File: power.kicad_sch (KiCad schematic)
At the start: 18 parts, among them J13 Screw_Terminal_01x02, U6 LM66100DCK, U7 LM66100DCK, U8 LMR51610XDBVR, U9 TLV74033PDBVR

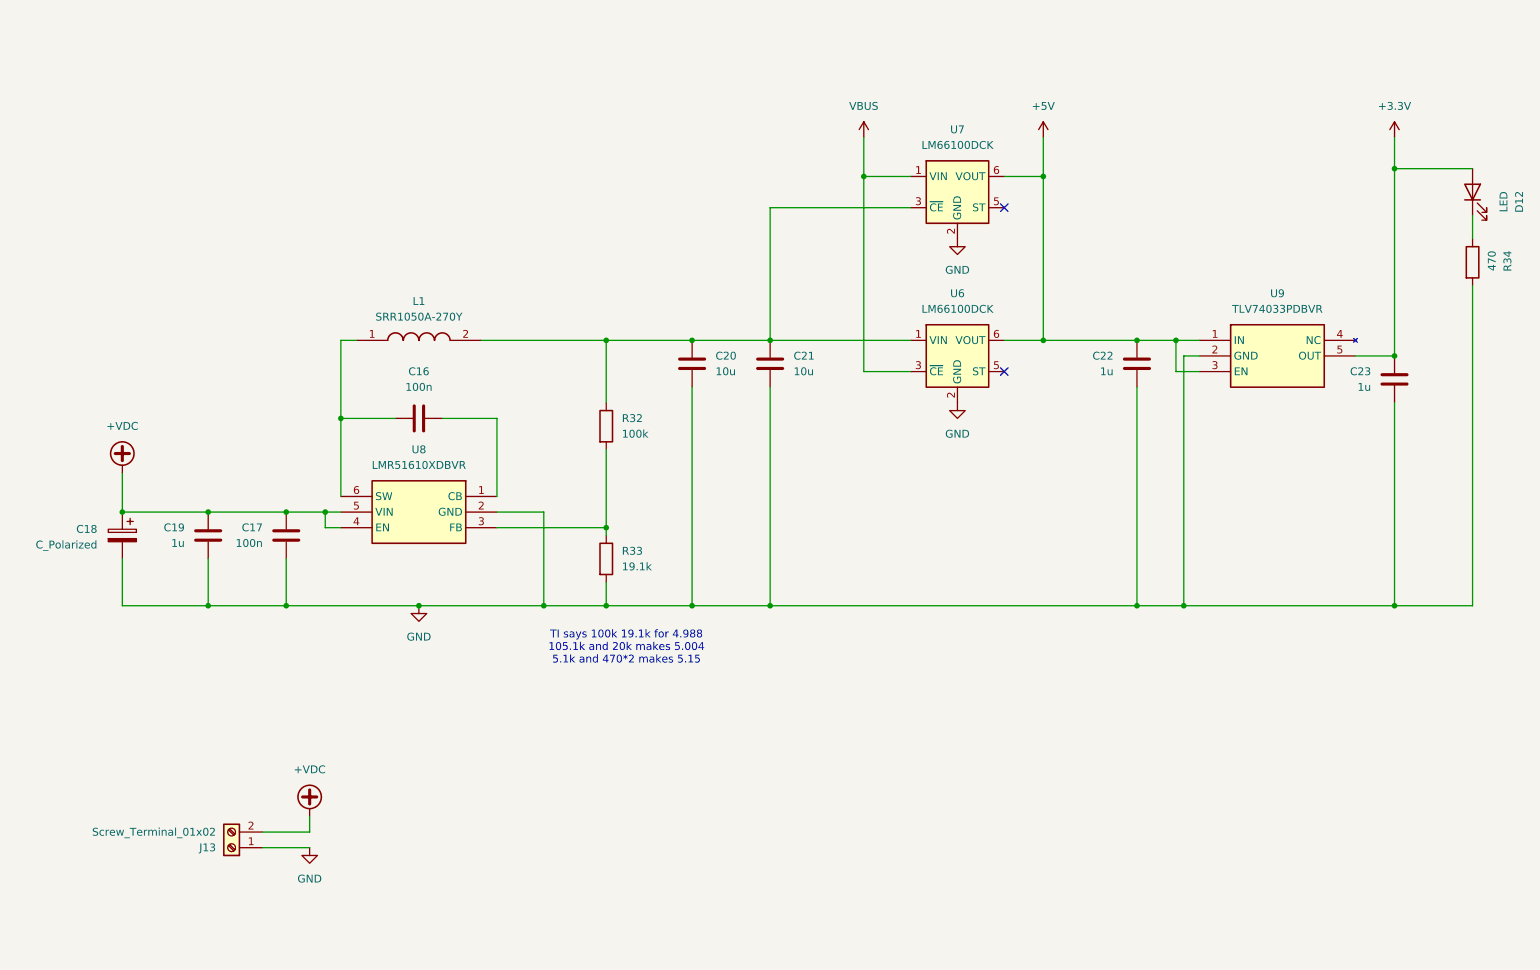
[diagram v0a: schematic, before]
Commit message: add probe headers
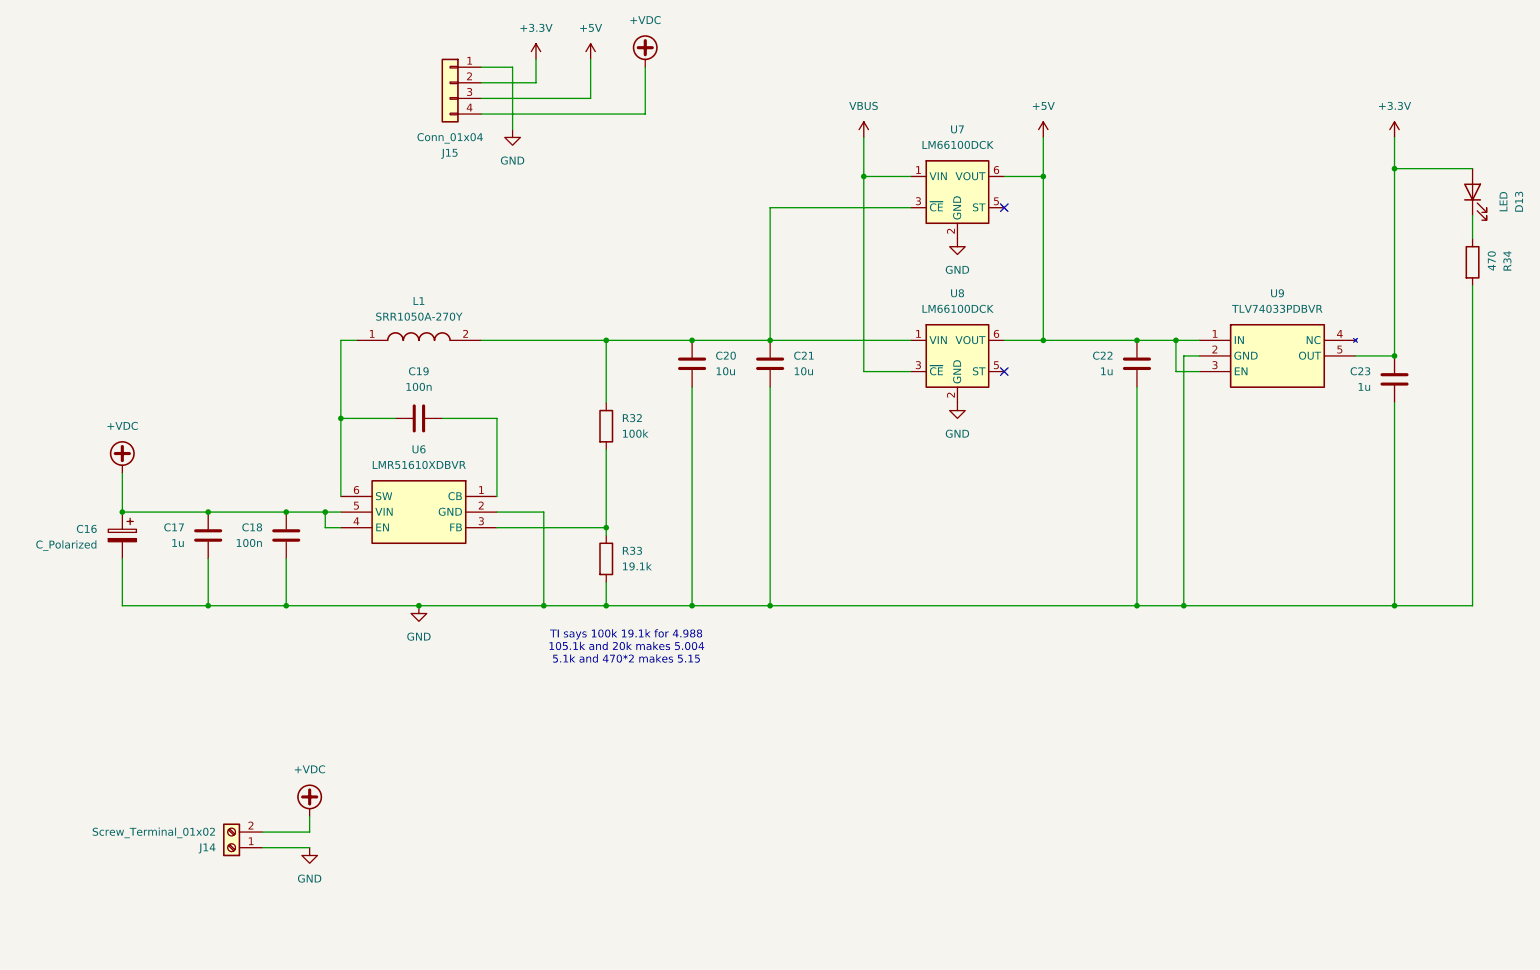
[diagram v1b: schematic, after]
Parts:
- added J15: Conn_01x04, Connector_PinHeader_2.54mm:PinHeader_1x04_P2.54mm_Vertical, symbol Connector_Generic:Conn_01x04
- renumbered C18 to C16, C19 to C17, C17 to C18, C16 to C19, D12 to D13, J13 to J14, U8 to U6, U6 to U8
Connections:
- net +3.3V: now also J15.2 (Pin_2)
- net +5V: now also J15.3 (Pin_3)
- net +VDC: now also J15.4 (Pin_4)
- net GND: now also J15.1 (Pin_1)

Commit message: partial layout
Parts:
- added C26: 100n, Capacitor_SMD:C_0603_1608Metric_Pad1.08x0.95mm_HandSolder, symbol Device:C
- added D14: MM3Zxx, Diode_SMD:D_SOD-323F, symbol Diode:MM3Zxx
- added R36: 100k, Resistor_SMD:R_0603_1608Metric_Pad0.98x0.95mm_HandSolder, symbol Device:R
- added R37: 5.1k, Resistor_SMD:R_0603_1608Metric_Pad0.98x0.95mm_HandSolder, symbol Device:R
- renumbered C16 to C18, C17 to C19, C18 to C20, C19 to C21, C20 to C22, C21 to C23, C22 to C24, C23 to C25, R32 to R33, R33 to R34, R34 to R35
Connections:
- net +VDC: now also R36.1
- net GND: now also C26.2, D14.2 (A), R37.2
- new net V_SENSE_VDC: C26.1, D14.1 (K), R36.2, R37.1

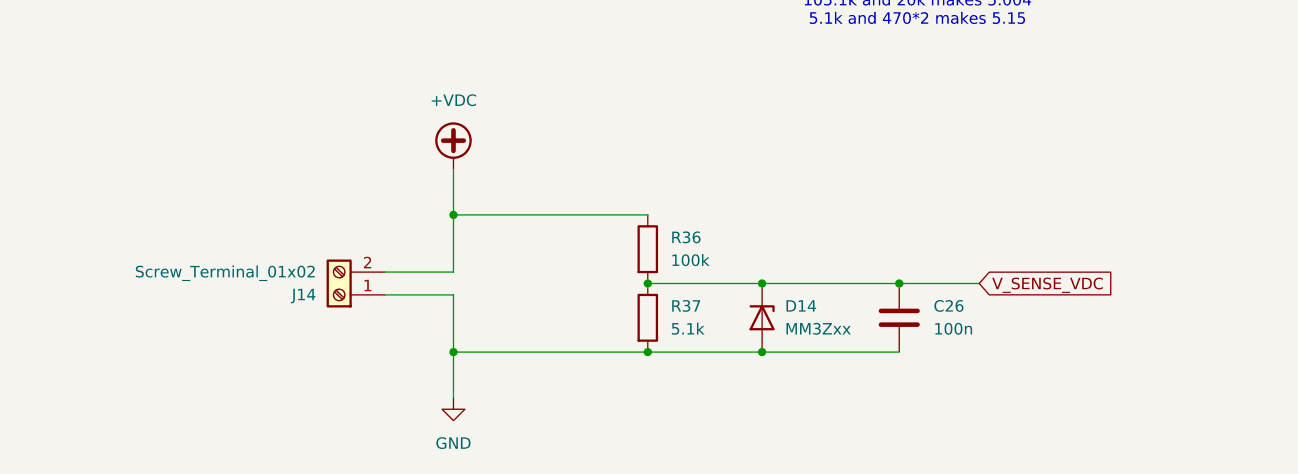
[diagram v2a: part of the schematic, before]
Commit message: schematic changes for mini
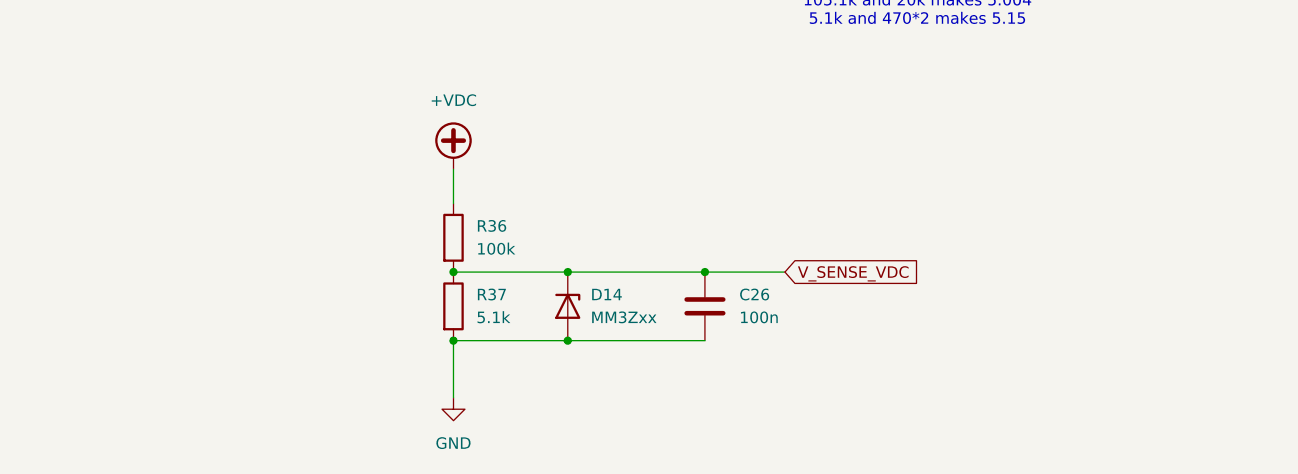
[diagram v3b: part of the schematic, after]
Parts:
- removed J14: Screw_Terminal_01x02, TerminalBlock_MetzConnect:TerminalBlock_MetzConnect_Type101_RT01602HBWC_1x02_P5.08mm_Horizontal, symbol Connector:Screw_Terminal_01x02
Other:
- moved on the sheet: C26, D14, R36, R37
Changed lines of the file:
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@@
 	)
 	(junction
-		(at 88.9 173.99)
+		(at 67.31 172.72)
 		(diameter 0)
 		(color 0 0 0 0)
@@
 	)
 	(junction
-		(at 101.6 173.99)
+		(at 80.01 172.72)
 		(diameter 0)
 		(color 0 0 0 0)
@@
 	)
 	(junction
-		(at 67.31 173.99)
-		(diameter 0)
-		(color 0 0 0 0)
-	)
-	(junction
 		(at 186.69 85.09)
 		(diameter 0)
@@
 	)
 	(junction
-		(at 116.84 166.37)
+		(at 95.25 165.1)
 		(diameter 0)
 		(color 0 0 0 0)
@@
 	)
 	(junction
-		(at 88.9 166.37)
+		(at 67.31 165.1)
 		(diameter 0)
 		(color 0 0 0 0)
@@
 	)
 	(junction
-		(at 101.6 166.37)
+		(at 80.01 165.1)
 		(diameter 0)
 		(color 0 0 0 0)
@@
 		(color 0 0 0 0)
 	)
-	(junction
-		(at 67.31 158.75)
-		(diameter 0)
-		(color 0 0 0 0)
-	)
 	(no_connect
 		(at 180.34 63.5)
@@
 	(wire
 		(pts
-			(xy 88.9 166.37) (xy 101.6 166.37)
+			(xy 67.31 165.1) (xy 80.01 165.1)
 		)
 		(stroke
@@
 	(wire
 		(pts
-			(xy 67.31 173.99) (xy 67.31 167.64)
-		)
-		(stroke
-			(width 0)
-			(type default)
-		)
-	)
-	(wire
-		(pts
 			(xy 142.24 92.71) (xy 142.24 128.27)
 		)
@@
 	(wire
 		(pts
-			(xy 59.69 165.1) (xy 67.31 165.1)
-		)
-		(stroke
-			(width 0)
-			(type default)
-		)
-	)
-	(wire
-		(pts
 			(xy 208.28 90.17) (xy 208.28 85.09)
 		)
@@
 	(wire
 		(pts
-			(xy 101.6 173.99) (xy 116.84 173.99)
+			(xy 80.01 172.72) (xy 95.25 172.72)
 		)
 		(stroke
@@
 	(wire
 		(pts
-			(xy 116.84 166.37) (xy 125.73 166.37)
+			(xy 95.25 165.1) (xy 104.14 165.1)
 		)
 		(stroke
@@
 	(wire
 		(pts
-			(xy 67.31 173.99) (xy 88.9 173.99)
-		)
-		(stroke
-			(width 0)
-			(type default)
-		)
-	)
-	(wire
-		(pts
-			(xy 67.31 158.75) (xy 67.31 153.67)
+			(xy 67.31 157.48) (xy 67.31 153.67)
 		)
 		(stroke
@@
 	(wire
 		(pts
-			(xy 67.31 165.1) (xy 67.31 158.75)
-		)
-		(stroke
-			(width 0)
-			(type default)
-		)
-	)
-	(wire
-		(pts
 			(xy 243.84 57.15) (xy 243.84 87.63)
 		)
@@
 	(wire
 		(pts
-			(xy 67.31 167.64) (xy 59.69 167.64)
-		)
-		(stroke
-			(width 0)
-			(type default)
-		)
-	)
-	(wire
-		(pts
 			(xy 180.34 85.09) (xy 186.69 85.09)
 		)
@@
 	(wire
 		(pts
-			(xy 101.6 166.37) (xy 116.84 166.37)
+			(xy 80.01 165.1) (xy 95.25 165.1)
 		)
 		(stroke
@@
 	(wire
 		(pts
-			(xy 67.31 179.07) (xy 67.31 173.99)
+			(xy 67.31 179.07) (xy 67.31 172.72)
 		)
 		(stroke
@@
 	(wire
 		(pts
-			(xy 88.9 173.99) (xy 101.6 173.99)
+			(xy 67.31 172.72) (xy 80.01 172.72)
 		)
 		(stroke
@@
 	(wire
 		(pts
-			(xy 67.31 158.75) (xy 88.9 158.75)
-		)
-		(stroke
-			(width 0)
-			(type default)
-		)
-	)
-	(wire
-		(pts
 			(xy 129.54 92.71) (xy 129.54 128.27)
 		)
@@
 	(global_label "V_SENSE_VDC"
 		(shape input)
-		(at 125.73 166.37 0)
+		(at 104.14 165.1 0)
 		(fields_autoplaced yes)
 		(effects
@@
 		)
 		(property "Intersheetrefs" "${INTERSHEET_REFS}"
-			(at 141.4151 166.37 0)
+			(at 119.8251 165.1 0)
 			(effects
 				(font
@@
 	(symbol
 		(lib_id "Diode:MM3Zxx")
-		(at 101.6 170.18 270)
+		(at 80.01 168.91 270)
 		(unit 1)
 		(exclude_from_sim no)
@@
 		(fields_autoplaced yes)
 		(property "Reference" "D14"
-			(at 104.14 168.9099 90)
+			(at 82.55 167.6399 90)
 			(effects
 				(font
@@
 		)
 		(property "Value" "MM3Zxx"
-			(at 104.14 171.4499 90)
+			(at 82.55 170.1799 90)
 			(effects
 				(font
@@
 		)
 		(property "Footprint" "Diode_SMD:D_SOD-323F"
-			(at 97.155 170.18 0)
+			(at 75.565 168.91 0)
 			(effects
 				(font
@@
 		)
 		(property "Datasheet" "https://diotec.com/tl_files/diotec/files/pdf/datasheets/mm3z2v4.pdf"
-			(at 101.6 170.18 0)
+			(at 80.01 168.91 0)
 			(effects
 				(font
@@
 		)
 		(property "Description" "300mW Zener Diode, SOD-323F"
-			(at 101.6 170.18 0)
+			(at 80.01 168.91 0)
 			(effects
 				(font
@@
 	(symbol
 		(lib_id "Device:R")
-		(at 88.9 170.18 0)
+		(at 67.31 168.91 0)
 		(unit 1)
 		(exclude_from_sim no)
@@
 		(fields_autoplaced yes)
 		(property "Reference" "R37"
-			(at 91.44 168.9099 0)
+			(at 69.85 167.6399 0)
 			(effects
 				(font
@@
 		)
 		(property "Value" "5.1k"
-			(at 91.44 171.4499 0)
+			(at 69.85 170.1799 0)
 			(effects
 				(font
@@
 		)
 		(property "Footprint" "Resistor_SMD:R_0603_1608Metric_Pad0.98x0.95mm_HandSolder"
-			(at 87.122 170.18 90)
+			(at 65.532 168.91 90)
 			(effects
 				(font
@@
 		)
 		(property "Datasheet" "~"
-			(at 88.9 170.18 0)
+			(at 67.31 168.91 0)
 			(effects
 				(font
@@
 		)
 		(property "Description" "Resistor"
-			(at 88.9 170.18 0)
+			(at 67.31 168.91 0)
 			(effects
 				(font
@@
 	(symbol
 		(lib_id "Device:C")
-		(at 116.84 170.18 0)
+		(at 95.25 168.91 0)
 		(unit 1)
 		(exclude_from_sim no)
@@
 		(fields_autoplaced yes)
 		(property "Reference" "C26"
-			(at 120.65 168.9099 0)
+			(at 99.06 167.6399 0)
 			(effects
 				(font
@@
 		)
 		(property "Value" "100n"
-			(at 120.65 171.4499 0)
+			(at 99.06 170.1799 0)
 			(effects
 				(font
@@
 		)
 		(property "Footprint" "Capacitor_SMD:C_0603_1608Metric_Pad1.08x0.95mm_HandSolder"
-			(at 117.8052 173.99 0)
+			(at 96.2152 172.72 0)
 			(effects
 				(font
@@
 		)
 		(property "Datasheet" "~"
-			(at 116.84 170.18 0)
+			(at 95.25 168.91 0)
 			(effects
 				(font
@@
 		)
 		(property "Description" "Unpolarized capacitor"
-			(at 116.84 170.18 0)
+			(at 95.25 168.91 0)
 			(effects
 				(font
@@
 	)
 	(symbol
-		(lib_id "Connector:Screw_Terminal_01x02")
-		(at 54.61 167.64 180)
-		(unit 1)
-		(exclude_from_sim no)
-		(in_bom yes)
-		(on_board yes)
-		(dnp no)
-		(property "Reference" "J14"
-			(at 52.07 167.6401 0)
-			(effects
-				(font
-					(size 1.27 1.27)
-				)
-				(justify left)
-			)
-		)
-		(property "Value" "Screw_Terminal_01x02"
-			(at 52.07 165.1001 0)
-			(effects
-				(font
-					(size 1.27 1.27)
-				)
-				(justify left)
-			)
-		)
-		(property "Footprint" "TerminalBlock_MetzConnect:TerminalBlock_MetzConnect_Type101_RT01602HBWC_1x02_P5.08mm_Horizontal"
-			(at 54.61 167.64 0)
-			(effects
-				(font
-					(size 1.27 1.27)
-				)
-				(hide yes)
-			)
-		)
-		(property "Datasheet" "~"
-			(at 54.61 167.64 0)
-			(effects
-				(font
-					(size 1.27 1.27)
-				)
-				(hide yes)
-			)
-		)
-		(property "Description" "Generic screw terminal, single row, 01x02, script generated (kicad-library-utils/schlib/autogen/connector/)"
-			(at 54.61 167.64 0)
-			(effects
-				(font
-					(size 1.27 1.27)
-				)
-				(hide yes)
-			)
-		)
-		(pin "2"
-		)
-		(pin "1"
-		)
-		(instances
-			(project "dmxdude"
-				(path "/bd7590c0-6a37-4bf0-a9f2-f26180744ceb/497bfd7a-c06a-4d4d-a320-8405be197f02"
-					(reference "J14")
-					(unit 1)
-				)
-			)
-		)
-	)
-	(symbol
 		(lib_id "Power_Management:LM66100DCK")
 		(at 172.72 60.96 0)
@@
 	(symbol
 		(lib_id "Device:R")
-		(at 88.9 162.56 0)
+		(at 67.31 161.29 0)
 		(unit 1)
 		(exclude_from_sim no)
@@
 		(fields_autoplaced yes)
 		(property "Reference" "R36"
-			(at 91.44 161.2899 0)
+			(at 69.85 160.0199 0)
 			(effects
 				(font
@@
 		)
 		(property "Value" "100k"
-			(at 91.44 163.8299 0)
+			(at 69.85 162.5599 0)
 			(effects
 				(font
@@
 		)
 		(property "Footprint" "Resistor_SMD:R_0603_1608Metric_Pad0.98x0.95mm_HandSolder"
-			(at 87.122 162.56 90)
+			(at 65.532 161.29 90)
 			(effects
 				(font
@@
 		)
 		(property "Datasheet" "~"
-			(at 88.9 162.56 0)
+			(at 67.31 161.29 0)
 			(effects
 				(font
@@
 		)
 		(property "Description" "Resistor"
-			(at 88.9 162.56 0)
+			(at 67.31 161.29 0)
 			(effects
 				(font
